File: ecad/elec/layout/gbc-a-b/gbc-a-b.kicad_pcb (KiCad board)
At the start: 2 copper layers, 5 parts

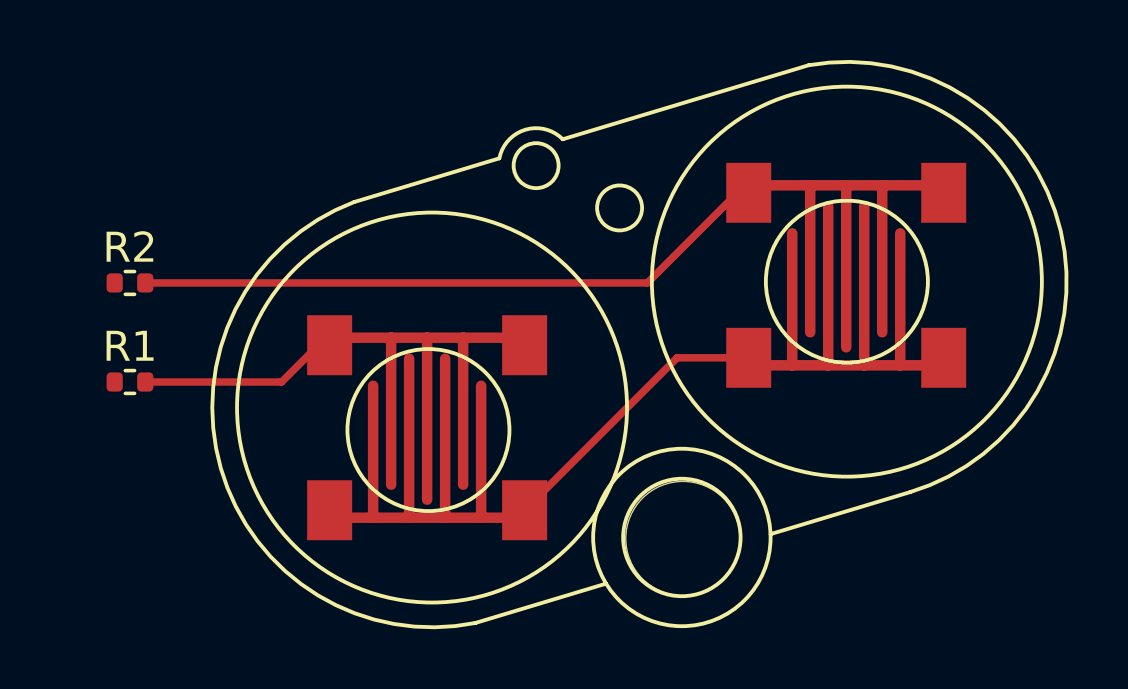
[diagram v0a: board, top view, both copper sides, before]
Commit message: Fix/atopile ecad (#82)
* fix(ecad): Fix bugs in atopile version of the design
* Add missing pullup resistors to AW9523 RSTN and INTN lines
* Fix I/O configuration for AW9523 so that all the inputs go to the same port pins as the previous version of the electronics

* minor cleanup to box3 after update to at 0.2.58

* fix udpate max17038 pullup to properly go to alert line after other fix

* typo

* update layout

* minor update to layout

* fix(buttons): pulldown -> pullup (so they are active low)

* update buttons to be pullup instead of pulldown; change led to be powered off VBUS instead of vbat

* update button footprints - start/select better aligned and all buttons have extra wires to ensure connections

* add net names and ensure packages are specified

* update box-emu-base layout

* update box-emu and box-3-emu layouts

* udpate to kicad 8

* add net name overrides and update all boards

* update atopile action to kicad 8

* comment out blender render
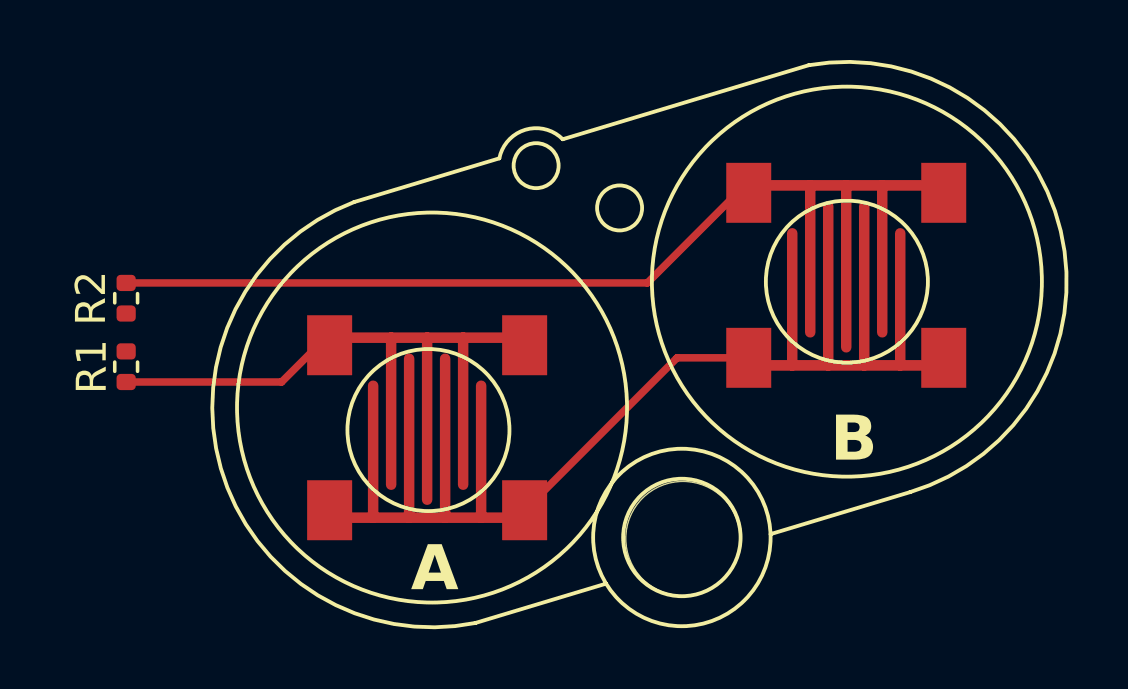
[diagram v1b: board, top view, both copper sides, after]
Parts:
- moved R1 0.53 mm to (144.7, 73.4), turned to -90 degrees
- moved R2 0.53 mm to (144.7, 71.1), turned to 90 degrees
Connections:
- R1 pad 1: gnd -> vcc
- R2 pad 1: gnd -> vcc
- U2 pad 2: vcc -> gnd
- U2 pad 4: vcc -> gnd
- U3 pad 2: vcc -> gnd
- U3 pad 4: vcc -> gnd
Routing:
- net gnd: track 0.00 -> 23.0 mm
- net vcc: track 9.57 -> 0.00 mm
- net a: track 6.28 -> 13.7 mm
- net b: track 21.0 -> 28.3 mm
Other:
- board text added: "A"
- board text added: "B"
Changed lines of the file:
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@@
   )
   (footprint "lib:R0402" (layer "F.Cu")
-    (at 144.78 73.914)
+    (at 144.653 71.122 90)
     (descr "Resistor SMD 0402 (1005 Metric), square (rectangular) end terminal, IPC_7351 nominal, (Body size source: IPC-SM-782 page 72, https://www.pcb-3d.com/wordpress/wp-content/uploads/ipc-sm-782a_amendment_1_and_2.pdf), generated with kicad-footprint-generator")
     (tags "resistor")
     (attr smd)
-    (fp_text reference "R1" (at 0 -1.17) (layer "F.SilkS")
+    (fp_text reference "R2" (at 0 -1.17 90) (layer "F.SilkS")
         (effects (font (size 1 1) (thickness 0.15)))
     )
-    (fp_text value "62.5mW Thick Film Resistors 50V ±100ppm/℃ ±1% 10kΩ 0402  Chip Resistor - Surface Mount ROHS" (at 0 1.17) (layer "F.Fab")
+    (fp_text value "62.5mW Thick Film Resistors 50V ±100ppm/℃ ±1% 10kΩ 0402  Chip Resistor - Surface Mount ROHS" (at 0 1.17 90) (layer "F.Fab")
         (effects (font (size 1 1) (thickness 0.15)))
     )
-    (fp_text user "${REFERENCE}" (at 0 0) (layer "F.Fab")
+    (fp_text user "${REFERENCE}" (at 0 0 90) (layer "F.Fab")
         (effects (font (size 0.26 0.26) (thickness 0.04)))
     )
@@
     (fp_line (start 0.525 0.27) (end -0.525 0.27)
       (stroke (width 0.1) (type solid)) (layer "F.Fab"))
-    (pad "1" smd roundrect (at -0.51 0) (size 0.54 0.64) (layers "F.Cu" "F.Paste" "F.Mask") (roundrect_rratio 0.25)
-      (net 1 "gnd") (pintype "stereo"))
-    (pad "2" smd roundrect (at 0.51 0) (size 0.54 0.64) (layers "F.Cu" "F.Paste" "F.Mask") (roundrect_rratio 0.25)
-      (net 2 "a") (pintype "stereo"))
+    (pad "1" smd roundrect (at -0.51 0 90) (size 0.54 0.64) (layers "F.Cu" "F.Paste" "F.Mask") (roundrect_rratio 0.25)
+      (net 4 "vcc") (pintype "stereo"))
+    (pad "2" smd roundrect (at 0.51 0 90) (size 0.54 0.64) (layers "F.Cu" "F.Paste" "F.Mask") (roundrect_rratio 0.25)
+      (net 3 "b") (pintype "stereo"))
     (model "${KICAD6_3DMODEL_DIR}/Resistor_SMD.3dshapes/R_0402_1005Metric.wrl"
       (offset (xyz 0 0 0))
@@
       (net 2 "a") (pintype "stereo") (solder_mask_margin 0.0635) (thermal_bridge_angle 0))
     (pad "2" smd rect (at -3.25 2.75) (size 1.5 2) (layers "F.Cu" "F.Paste" "F.Mask")
-      (net 4 "vcc") (pintype "stereo") (solder_mask_margin 0.0635) (thermal_bridge_angle 0))
+      (net 1 "gnd") (pintype "stereo") (solder_mask_margin 0.0635) (thermal_bridge_angle 0))
     (pad "3" smd rect (at 3.25 -2.75) (size 1.5 2) (layers "F.Cu" "F.Paste" "F.Mask")
       (net 2 "a") (pintype "stereo") (solder_mask_margin 0.0635) (thermal_bridge_angle 0))
     (pad "4" smd rect (at 3.25 2.75) (size 1.5 2) (layers "F.Cu" "F.Paste" "F.Mask")
-      (net 4 "vcc") (pintype "stereo") (solder_mask_margin 0.0635) (thermal_bridge_angle 0))
+      (net 1 "gnd") (pintype "stereo") (solder_mask_margin 0.0635) (thermal_bridge_angle 0))
   )
   (footprint "lib:R0402" (layer "F.Cu")
-    (at 144.78 70.612)
+    (at 144.653 73.404 -90)
     (descr "Resistor SMD 0402 (1005 Metric), square (rectangular) end terminal, IPC_7351 nominal, (Body size source: IPC-SM-782 page 72, https://www.pcb-3d.com/wordpress/wp-content/uploads/ipc-sm-782a_amendment_1_and_2.pdf), generated with kicad-footprint-generator")
     (tags "resistor")
     (attr smd)
-    (fp_text reference "R2" (at 0 -1.17) (layer "F.SilkS")
+    (fp_text reference "R1" (at -0.002 1.143 90) (layer "F.SilkS")
         (effects (font (size 1 1) (thickness 0.15)))
     )
-    (fp_text value "62.5mW Thick Film Resistors 50V ±100ppm/℃ ±1% 10kΩ 0402  Chip Resistor - Surface Mount ROHS" (at 0 1.17) (layer "F.Fab")
+    (fp_text value "62.5mW Thick Film Resistors 50V ±100ppm/℃ ±1% 10kΩ 0402  Chip Resistor - Surface Mount ROHS" (at 0 1.17 90) (layer "F.Fab")
         (effects (font (size 1 1) (thickness 0.15)))
     )
-    (fp_text user "${REFERENCE}" (at 0 0) (layer "F.Fab")
+    (fp_text user "${REFERENCE}" (at 0 0 90) (layer "F.Fab")
         (effects (font (size 0.26 0.26) (thickness 0.04)))
     )
@@
     (fp_line (start 0.525 0.27) (end -0.525 0.27)
       (stroke (width 0.1) (type solid)) (layer "F.Fab"))
-    (pad "1" smd roundrect (at -0.51 0) (size 0.54 0.64) (layers "F.Cu" "F.Paste" "F.Mask") (roundrect_rratio 0.25)
-      (net 1 "gnd") (pintype "stereo"))
-    (pad "2" smd roundrect (at 0.51 0) (size 0.54 0.64) (layers "F.Cu" "F.Paste" "F.Mask") (roundrect_rratio 0.25)
-      (net 3 "b") (pintype "stereo"))
+    (pad "1" smd roundrect (at -0.51 0 270) (size 0.54 0.64) (layers "F.Cu" "F.Paste" "F.Mask") (roundrect_rratio 0.25)
+      (net 4 "vcc") (pintype "stereo"))
+    (pad "2" smd roundrect (at 0.51 0 270) (size 0.54 0.64) (layers "F.Cu" "F.Paste" "F.Mask") (roundrect_rratio 0.25)
+      (net 2 "a") (pintype "stereo"))
     (model "${KICAD6_3DMODEL_DIR}/Resistor_SMD.3dshapes/R_0402_1005Metric.wrl"
       (offset (xyz 0 0 0))
@@
       (net 3 "b") (pintype "stereo") (solder_mask_margin 0.0635) (thermal_bridge_angle 0))
     (pad "2" smd rect (at -3.25 2.75) (size 1.5 2) (layers "F.Cu" "F.Paste" "F.Mask")
-      (net 4 "vcc") (pintype "stereo") (solder_mask_margin 0.0635) (thermal_bridge_angle 0))
+      (net 1 "gnd") (pintype "stereo") (solder_mask_margin 0.0635) (thermal_bridge_angle 0))
     (pad "3" smd rect (at 3.25 -2.75) (size 1.5 2) (layers "F.Cu" "F.Paste" "F.Mask")
       (net 3 "b") (pintype "stereo") (solder_mask_margin 0.0635) (thermal_bridge_angle 0))
     (pad "4" smd rect (at 3.25 2.75) (size 1.5 2) (layers "F.Cu" "F.Paste" "F.Mask")
-      (net 4 "vcc") (pintype "stereo") (solder_mask_margin 0.0635) (thermal_bridge_angle 0))
-  )
+      (net 1 "gnd") (pintype "stereo") (solder_mask_margin 0.0635) (thermal_bridge_angle 0))
+  )
+  (gr_text "A" (at 154.94 79.248) (layer "F.SilkS")
+    (effects (font (size 1.5 1.5) (thickness 0.3) bold) (justify top))
+  )
+  (gr_text "B" (at 168.91 74.93) (layer "F.SilkS")
+    (effects (font (size 1.5 1.5) (thickness 0.3) bold) (justify top))
+  )
+  (segment (start 165.406 73.108) (end 163.016 73.108) (width 0.25) (layer "F.Cu") (net 1))
+  (segment (start 151.436 78.188) (end 151.788 78.188) (width 0.25) (layer "F.Cu") (net 1))
+  (segment (start 165.406 73.108) (end 165.698 73.4) (width 0.25) (layer "F.Cu") (net 1))
+  (segment (start 152 78.4) (end 157.724 78.4) (width 0.25) (layer "F.Cu") (net 1))
+  (segment (start 157.724 78.4) (end 157.936 78.188) (width 0.25) (layer "F.Cu") (net 1))
+  (segment (start 171.614 73.4) (end 171.906 73.108) (width 0.25) (layer "F.Cu") (net 1))
+  (segment (start 151.788 78.188) (end 152 78.4) (width 0.25) (layer "F.Cu") (net 1))
+  (segment (start 165.698 73.4) (end 171.614 73.4) (width 0.25) (layer "F.Cu") (net 1))
+  (segment (start 163.016 73.108) (end 157.936 78.188) (width 0.25) (layer "F.Cu") (net 1))
+  (segment (start 151.436 72.688) (end 151.912 72.688) (width 0.25) (layer "F.Cu") (net 2))
   (segment (start 149.835 73.914) (end 151.061 72.688) (width 0.25) (layer "F.Cu") (net 2))
-  (segment (start 145.29 73.914) (end 149.835 73.914) (width 0.25) (layer "F.Cu") (net 2))
+  (segment (start 152.2 72.4) (end 157.648 72.4) (width 0.25) (layer "F.Cu") (net 2))
+  (segment (start 157.648 72.4) (end 157.936 72.688) (width 0.25) (layer "F.Cu") (net 2))
+  (segment (start 151.912 72.688) (end 152.2 72.4) (width 0.25) (layer "F.Cu") (net 2))
+  (segment (start 144.653 73.914) (end 149.835 73.914) (width 0.25) (layer "F.Cu") (net 2))
   (segment (start 162.027 70.612) (end 165.031 67.608) (width 0.25) (layer "F.Cu") (net 3))
-  (segment (start 145.29 70.612) (end 162.027 70.612) (width 0.25) (layer "F.Cu") (net 3))
-  (segment (start 165.406 73.108) (end 163.016 73.108) (width 0.25) (layer "F.Cu") (net 4))
-  (segment (start 163.016 73.108) (end 157.936 78.188) (width 0.25) (layer "F.Cu") (net 4))
+  (segment (start 144.653 70.612) (end 162.027 70.612) (width 0.25) (layer "F.Cu") (net 3))
+  (segment (start 165.406 67.608) (end 165.614 67.4) (width 0.25) (layer "F.Cu") (net 3))
+  (segment (start 165.614 67.4) (end 171.698 67.4) (width 0.25) (layer "F.Cu") (net 3))
+  (segment (start 171.698 67.4) (end 171.906 67.608) (width 0.25) (layer "F.Cu") (net 3))
   (group "" (id 3d9968b9-117e-4bfe-8f96-8323dd130617)
     (members
-      13ac4102-857c-41e8-8c67-279c0f1f3b8d
-      16b8e84e-8626-422d-935f-05c00c67cbea
       229863ec-9668-45f0-9ed6-19d280119f1b
-      2f49c7f8-4dae-4ec8-97fe-db874cf1deeb
       66744fc4-8100-43f2-a509-1b98d8613cd6
-      947244d6-5e9b-4847-82c2-f463b99eb6de
       ae0bef5c-a94e-4962-a6a0-12f651a7892f
-      b578f6b0-2556-4860-8664-f45da851e50f
       d632ad78-7f69-4103-aada-2a6a5e2f1179
-      df468f08-1c50-4708-989c-4c1735339442
       f0479198-c696-4f75-9253-c1ee8e13ea77
     )
